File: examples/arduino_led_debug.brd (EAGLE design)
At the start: 160 x 100 mm, 3 parts

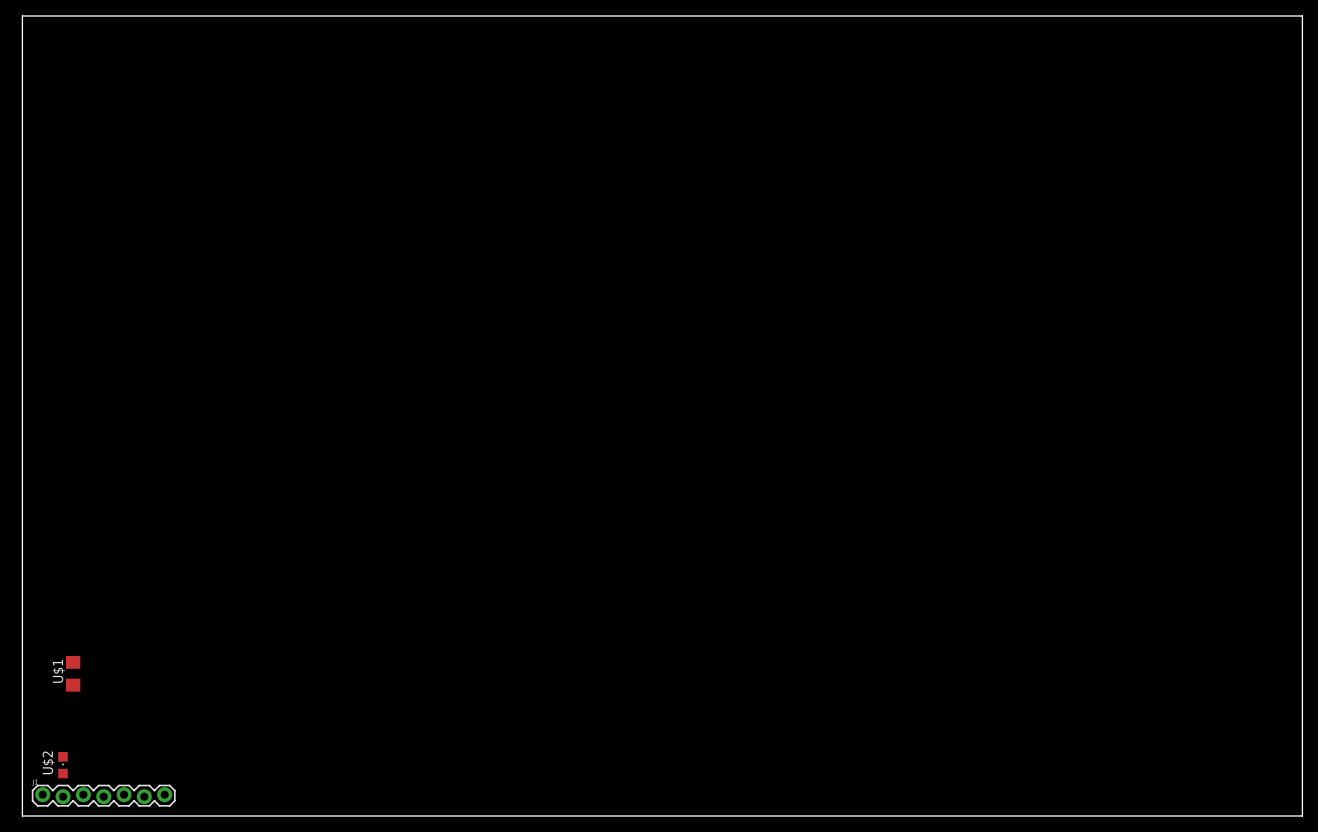
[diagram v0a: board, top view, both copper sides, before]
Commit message: Improving library. Still no real LED library! Added example project to test ULPs against.
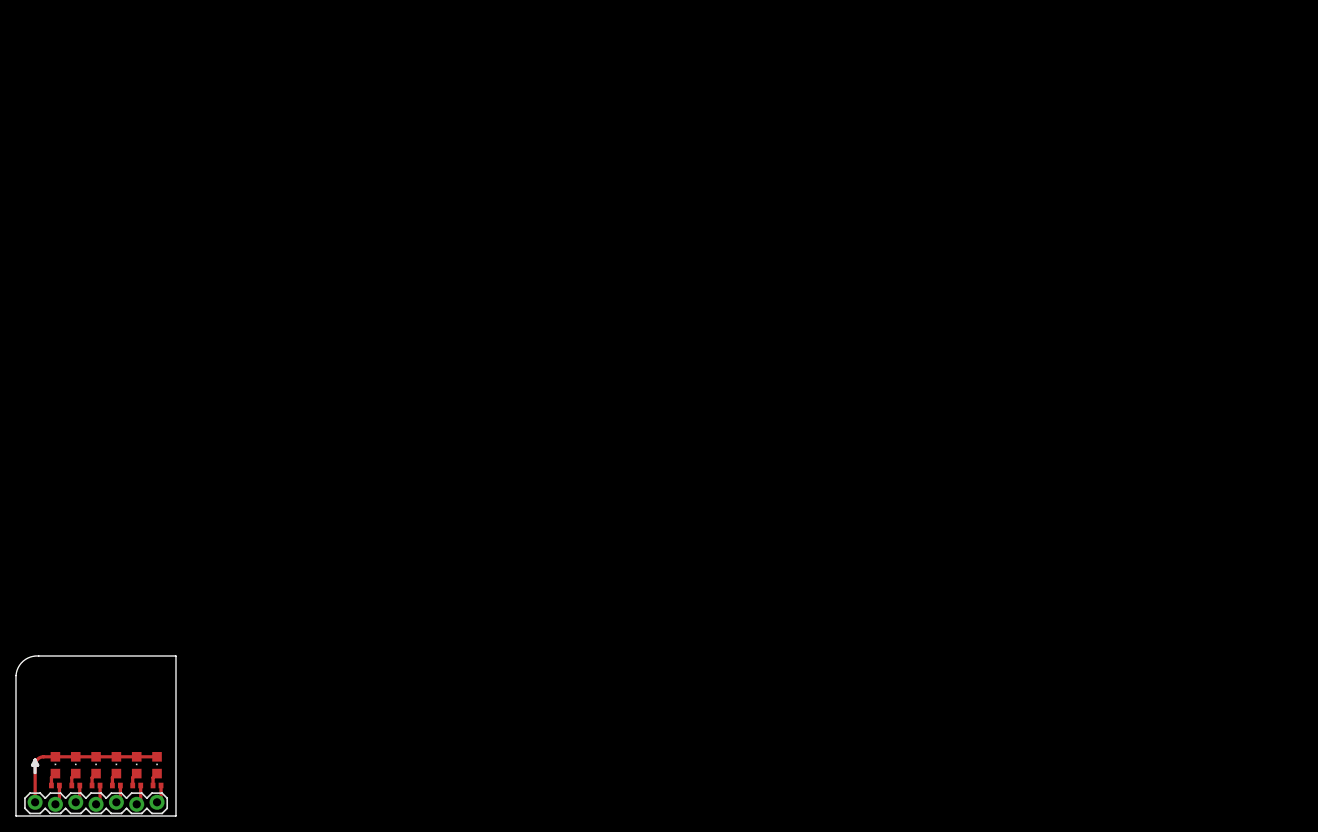
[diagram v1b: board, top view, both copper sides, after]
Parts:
- removed U$1: 1KΩ(1001)_±0.1%_C95522*1KΩ(1001)_±0.1%_C95522_1206, Resistors:RESISTOR_1206
- removed U$2: 17-21/R6C-AQ2R2B/3T*C113551_17-21/R6C-AQ2R2B/3T_0805, Optocouplers & LEDs & Infrared:LED_0805
- added D1, D2, D3, D4, D5, D6: 17-21/R6C-AQ2R2B/3T, Optocouplers & LEDs & Infrared.expanded:LED_0805
- added R1, R2, R3, R4, R5, R6: 1KΩ, Resistors.basic:RESISTOR_0402
- moved J1 1.35 mm to (1.59, 1.59)
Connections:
- new net N$1: D1.A, R1.1
- new net N$11: D5.A, R5.1
- new net N$12: D6.A, R6.1
- new net N$2: D2.A, R2.1
- new net N$3: D3.A, R3.1
- new net N$5: D4.A, R4.1
- net GND: now also D1.C, D2.C, D3.C, D4.C, D5.C, D6.C
- net N$10: now also R2.2
- net N$4: now also R1.2
- net N$6: now also R6.2
- net N$7: now also R5.2
- net N$8: now also R4.2
- net N$9: now also R3.2
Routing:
- net GND: track 0.00 -> 20.3 mm
- net N$8: track 0.00 -> 2.56 mm
- net N$6: track 0.00 -> 2.56 mm
- net N$10: track 0.00 -> 2.56 mm
- net N$9: track 0.00 -> 2.30 mm
- net N$7: track 0.00 -> 2.30 mm
- net N$4: track 0.00 -> 2.30 mm
- net N$12: track 0.00 -> 1.70 mm
- net N$5: track 0.00 -> 1.70 mm
- net N$3: track 0.00 -> 1.70 mm
- net N$2: track 0.00 -> 1.70 mm
- net N$11: track 0.00 -> 1.70 mm
- net N$1: track 0.00 -> 1.70 mm
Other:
- board size 160 x 100 mm -> 20 x 20 mm
